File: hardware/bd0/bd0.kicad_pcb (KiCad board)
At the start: 2 copper layers, 136.5 x 104 mm, 24 parts, among them J1 USB_C_Receptacle_USB2.0, J2 SJ-43514, U1 ATSAMD21G15B-A

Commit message: Finished BD0 schematic and routing
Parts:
- added C1: 1uF, Capacitor_SMD:C_0603_1608Metric, F.Cu at (222.0, 159.0)
- added C2: 0.1uF, Capacitor_SMD:C_0603_1608Metric, F.Cu at (215.5, 165.9)
- added C3: 0.1uF, Capacitor_SMD:C_0603_1608Metric, F.Cu at (222.0, 157.5)
- added C4: 0.1uF, Capacitor_SMD:C_0603_1608Metric, F.Cu at (228.5, 162.7)
- added C5: 0.1uF, Capacitor_SMD:C_0603_1608Metric, F.Cu at (221.5, 172.5)
- added C6: 10uF, Capacitor_SMD:C_0603_1608Metric, F.Cu at (221.5, 174.0)
- added C7: 10uF, Capacitor_SMD:C_0603_1608Metric, F.Cu at (214.0, 165.9)
- added C8: 1uF, Capacitor_SMD:C_0603_1608Metric, F.Cu at (238.0, 162.7)
- added C9: 1uF, Capacitor_SMD:C_0603_1608Metric, F.Cu at (236.8, 160.2)
- added D1: LED, Diode_SMD:D_0603_1608Metric, B.Cu at (273.2, 139.5)
- added D2: LED, Diode_SMD:D_0603_1608Metric, B.Cu at (273.2, 136.0)
- added D3: LED, Diode_SMD:D_0603_1608Metric, B.Cu at (273.2, 132.5)
- added FB1: FerriteBead, Inductor_SMD:L_0603_1608Metric, F.Cu at (212.5, 167.4)
- added J20: USB_C_Receptacle_USB2.0, Connector_USB:USB_C_Receptacle_JAE_DX07S016JA1R1500, B.Cu at (273.2, 109.6)
- added J3: SJ-43514, Conn_CUI_SJ-4351:CUI-SJ-43514-SMT-0, F.Cu at (271.1, 165.2)
- added J30: SJ-43514, Conn_CUI_SJ-4351:CUI-SJ-43514-SMT-0, B.Cu at (271.1, 165.9)
- added R1: 10k, Resistor_SMD:R_0603_1608Metric, F.Cu at (225.3, 159.0)
- added R2: 1k, Resistor_SMD:R_0603_1608Metric, F.Cu at (219.5, 158.2)
- added R3: 10k, Resistor_SMD:R_0603_1608Metric, F.Cu at (261.0, 166.6)
- added R4: 10k, Resistor_SMD:R_0603_1608Metric, F.Cu at (261.0, 163.2)
- added R5: 470, Resistor_SMD:R_0603_1608Metric, B.Cu at (273.2, 141.1)
- added R6: 470, Resistor_SMD:R_0603_1608Metric, B.Cu at (273.2, 137.6)
- added R7: 470, Resistor_SMD:R_0603_1608Metric, B.Cu at (273.2, 134.1)
- added U2: AP2127N-3.3, Package_TO_SOT_SMD:SOT-23, F.Cu at (235.0, 162.7)
- J1: value USB_C_Receptacle_USB2.0 -> Conn_02x03_Odd_Even; footprint Connector_USB:USB_C_Receptacle_JAE_DX07S016JA1R1500 -> Connector:Tag-Connect_TC2030-IDC-NL_2x03_P1.27mm_Vertical
- J2: value SJ-43514 -> USB_C_Receptacle_USB2.0; footprint Conn_CUI_SJ-4351:CUI-SJ-43514-0 -> Connector_USB:USB_C_Receptacle_JAE_DX07S016JA1R1500
- moved J1 64.7 mm to (216.0, 158.5), turned to -90 degrees
- moved J2 59.7 mm to (273.2, 109.6)
- moved S20 11.6 mm to (263.4, 183.2), turned to -115 degrees
- moved S10 11.6 mm to (222.0, 143.0)
- moved S11 11.6 mm to (222.0, 126.0)
- moved S12 11.6 mm to (222.0, 109.0)
- moved S13 11.6 mm to (240.0, 150.0)
- moved S14 11.6 mm to (240.0, 133.0)
- moved S15 11.6 mm to (240.0, 116.0)
- moved S16 11.6 mm to (258.0, 150.0)
- moved S17 11.6 mm to (258.0, 133.0)
- moved S18 11.6 mm to (258.0, 116.0)
- moved S19 11.6 mm to (248.0, 176.0), turned to -115 degrees
- moved S21 11.6 mm to (278.8, 190.4), turned to -115 degrees
- moved U1 11.6 mm to (222.0, 166.0)
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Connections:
- S1 pad 1: GND -> /outer_bottom
- S1 pad 2: /outer_bottom -> GND
- S10 pad 1: GND -> /middle_bottom
- S10 pad 2: /middle_bottom -> GND
- S11 pad 1: GND -> /middle_home
- S11 pad 2: /middle_home -> GND
- S12 pad 1: GND -> /middle_top
- S12 pad 2: /middle_top -> GND
- S13 pad 1: GND -> /index_bottom
- S13 pad 2: /index_bottom -> GND
- S14 pad 1: GND -> /index_home
- S14 pad 2: /index_home -> GND
- S15 pad 1: GND -> /index_top
- S15 pad 2: /index_top -> GND
- S16 pad 1: GND -> /inner_bottom
- S16 pad 2: /inner_bottom -> GND
- S17 pad 1: GND -> /inner_home
- S17 pad 2: /inner_home -> GND
- S18 pad 1: GND -> /inner_top
- S18 pad 2: /inner_top -> GND
- S19 pad 1: GND -> /near_thumb
- S19 pad 2: /near_thumb -> GND
- S2 pad 1: GND -> /outer_home
- S2 pad 2: /outer_home -> GND
- S20 pad 1: GND -> /home_thumb
- S20 pad 2: /home_thumb -> GND
- S21 pad 1: GND -> /far_thumb
- S21 pad 2: /far_thumb -> GND
- S3 pad 1: GND -> /outer_top
- S3 pad 2: /outer_top -> GND
- S4 pad 1: GND -> /pinky_bottom
- S4 pad 2: /pinky_bottom -> GND
- S5 pad 1: GND -> /pinky_home
- S5 pad 2: /pinky_home -> GND
- S6 pad 1: GND -> /pinky_top
- S6 pad 2: /pinky_top -> GND
- S7 pad 1: GND -> /ring_bottom
- S7 pad 2: /ring_bottom -> GND
- S8 pad 1: GND -> /ring_home
- S8 pad 2: /ring_home -> GND
- S9 pad 1: GND -> /ring_top
- S9 pad 2: /ring_top -> GND
- U1 pad 10: unconnected-(U1-Pad10) -> /middle_top
- U1 pad 11: unconnected-(U1-Pad11) -> /ring_bottom
- U1 pad 12: unconnected-(U1-Pad12) -> /ring_home
- U1 pad 13: /home_thumb -> /near_thumb
- U1 pad 14: unconnected-(U1-Pad14) -> /ring_top
- U1 pad 15: unconnected-(U1-Pad15) -> /pinky_bottom
- U1 pad 16: unconnected-(U1-Pad16) -> /pinky_home
- U1 pad 17: unconnected-(U1-Pad17) -> +3V3
- U1 pad 2: unconnected-(U1-Pad2) -> /index_home
- U1 pad 21: unconnected-(U1-Pad21) -> /pinky_top
- U1 pad 22: unconnected-(U1-Pad22) -> /outer_bottom
- U1 pad 23: unconnected-(U1-Pad23) -> /outer_home
- U1 pad 24: unconnected-(U1-Pad24) -> /outer_top
- U1 pad 25: unconnected-(U1-Pad25) -> /home_thumb
- U1 pad 26: unconnected-(U1-Pad26) -> /far_thumb
- U1 pad 27: unconnected-(U1-Pad27) -> /inner_bottom
- U1 pad 28: unconnected-(U1-Pad28) -> /inner_home
- U1 pad 29: unconnected-(U1-Pad29) -> /inner_top
- U1 pad 3: unconnected-(U1-Pad3) -> /index_top
- U1 pad 30: /RX -> unconnected-(U1-Pad30)
- U1 pad 31: /TX -> /SDA
- U1 pad 32: unconnected-(U1-Pad32) -> /SCL
- U1 pad 33: /USB_DM -> /USB_DN
- U1 pad 36: unconnected-(U1-Pad36) -> +3V3
- U1 pad 37: unconnected-(U1-Pad37) -> /LED0
- U1 pad 38: unconnected-(U1-Pad38) -> /LED1
- U1 pad 39: unconnected-(U1-Pad39) -> /LED2
- U1 pad 4: unconnected-(U1-Pad4) -> /middle_bottom
- U1 pad 40: unconnected-(U1-Pad40) -> /RESETn
- U1 pad 41: unconnected-(U1-Pad41) -> /index_bottom
- U1 pad 43: unconnected-(U1-Pad43) -> +1V2
- U1 pad 44: unconnected-(U1-Pad44) -> +3V3
- U1 pad 45: unconnected-(U1-Pad45) -> /SWCLK
- U1 pad 46: unconnected-(U1-Pad46) -> /SWDIO
- U1 pad 6: unconnected-(U1-Pad6) -> /3V3A
- U1 pad 9: unconnected-(U1-Pad9) -> /middle_home
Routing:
- net /outer_top: track 0.00 -> 115.9 mm, vias 0 -> 1
- net +3V3: track 0.00 -> 104.3 mm, vias 0 -> 8
- net /outer_home: track 0.00 -> 97.3 mm, vias 0 -> 1
- net /pinky_top: track 0.00 -> 97.2 mm, vias 0 -> 1
- net /USB_DN: track 0.00 -> 95.1 mm, vias 0 -> 1
- net +5V: track 0.00 -> 91.4 mm, vias 0 -> 1
- net /USB_DP: track 0.00 -> 91.1 mm, vias 0 -> 1
- net /inner_top: track 0.00 -> 86.5 mm, vias 0 -> 3
- net /index_top: track 0.00 -> 85.4 mm, vias 0 -> 1
- net /middle_top: track 0.00 -> 83.3 mm, vias 0 -> 1
- net /ring_top: track 0.00 -> 81.8 mm, vias 0 -> 1
- net GND: track 0.00 -> 79.4 mm, vias 0 -> 28
- net /outer_bottom: track 0.00 -> 79.0 mm, vias 0 -> 1
- net /far_thumb: track 0.00 -> 71.6 mm, vias 0 -> 1
- net /pinky_home: track 0.00 -> 71.5 mm, vias 0 -> 1
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- added copper zone on B.Cu, net GND
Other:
- board size 136.5 x 104 mm -> 138.2 x 104.9 mm

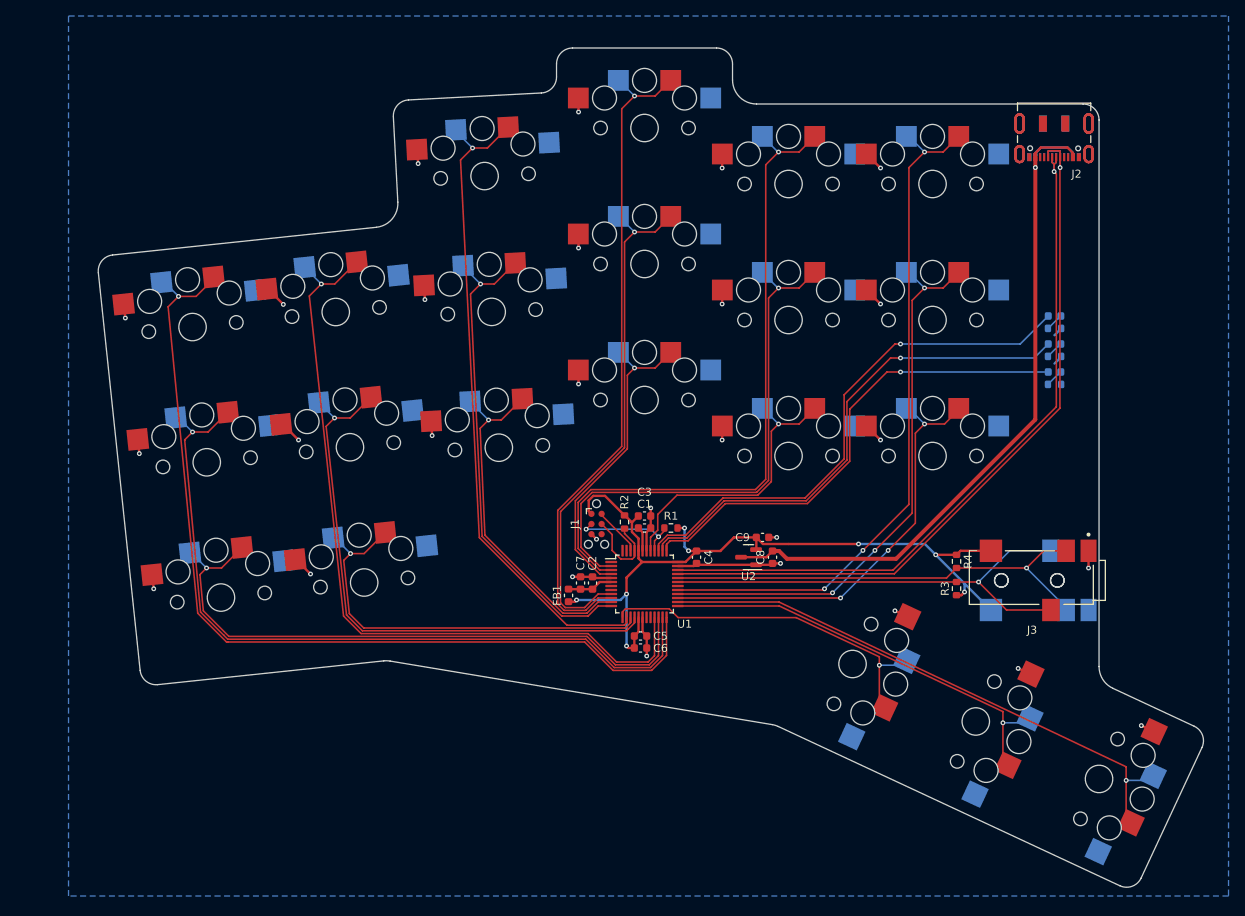
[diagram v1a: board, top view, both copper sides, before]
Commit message: Edit local USB-C footprint to meet DRC
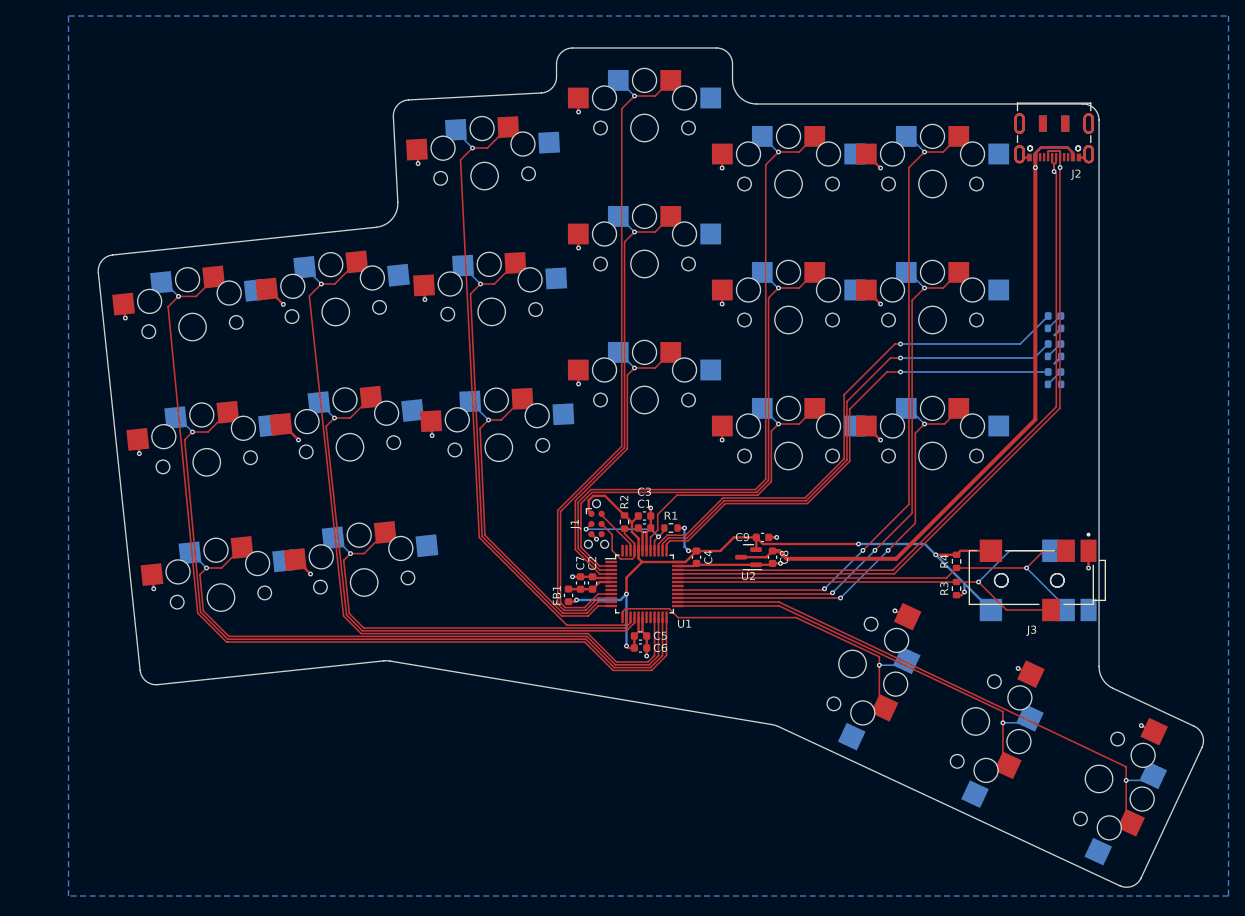
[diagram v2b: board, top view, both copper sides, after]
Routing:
- net GND: track 79.4 -> 80.4 mm

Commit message: Add signature and output generation
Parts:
- added G***: LOGO, lib:Signature, B.Cu at (217.1, 174.1)
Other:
- rule pad_to_mask_clearance: 0.05 -> 0
- board text added: "JLCJLCJLCJLC"
